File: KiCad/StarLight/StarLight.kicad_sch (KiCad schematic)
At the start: 17 parts, among them Q1 Q_NPN, Q2 Q_NPN, Q3 Q_NPN, SW1 SW, SW2 SW

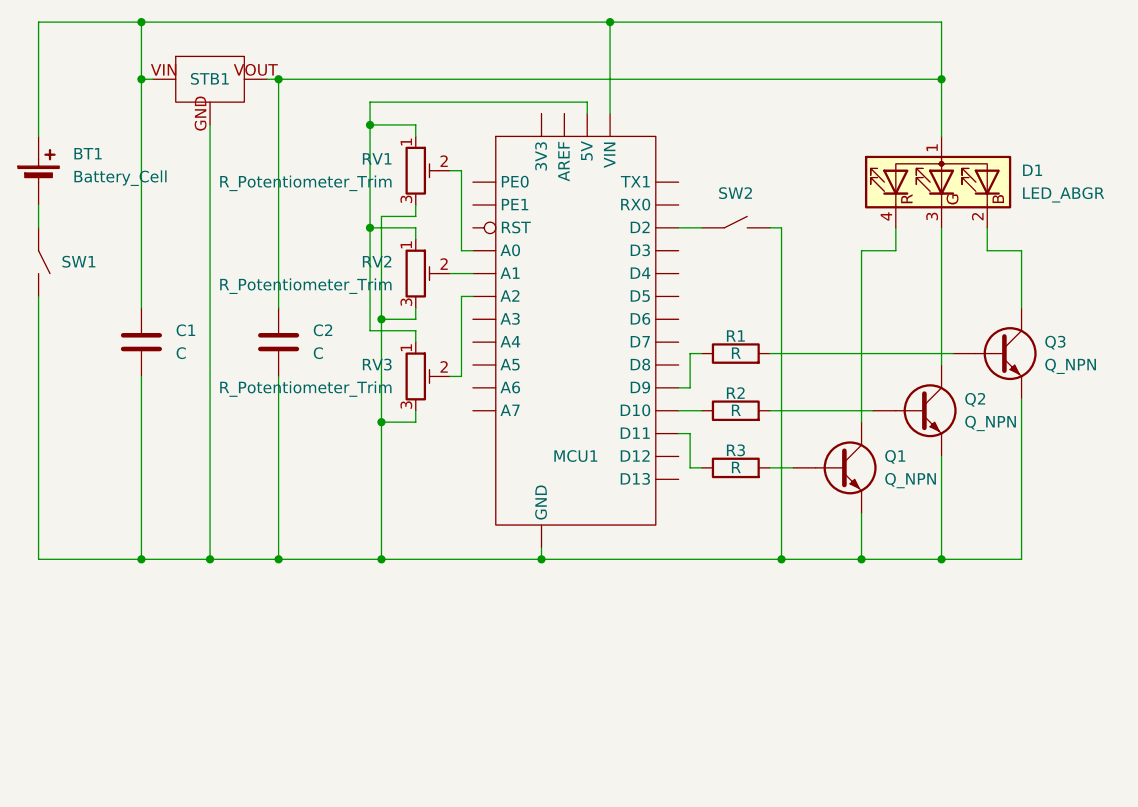
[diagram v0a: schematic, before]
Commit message: Create layout for elements
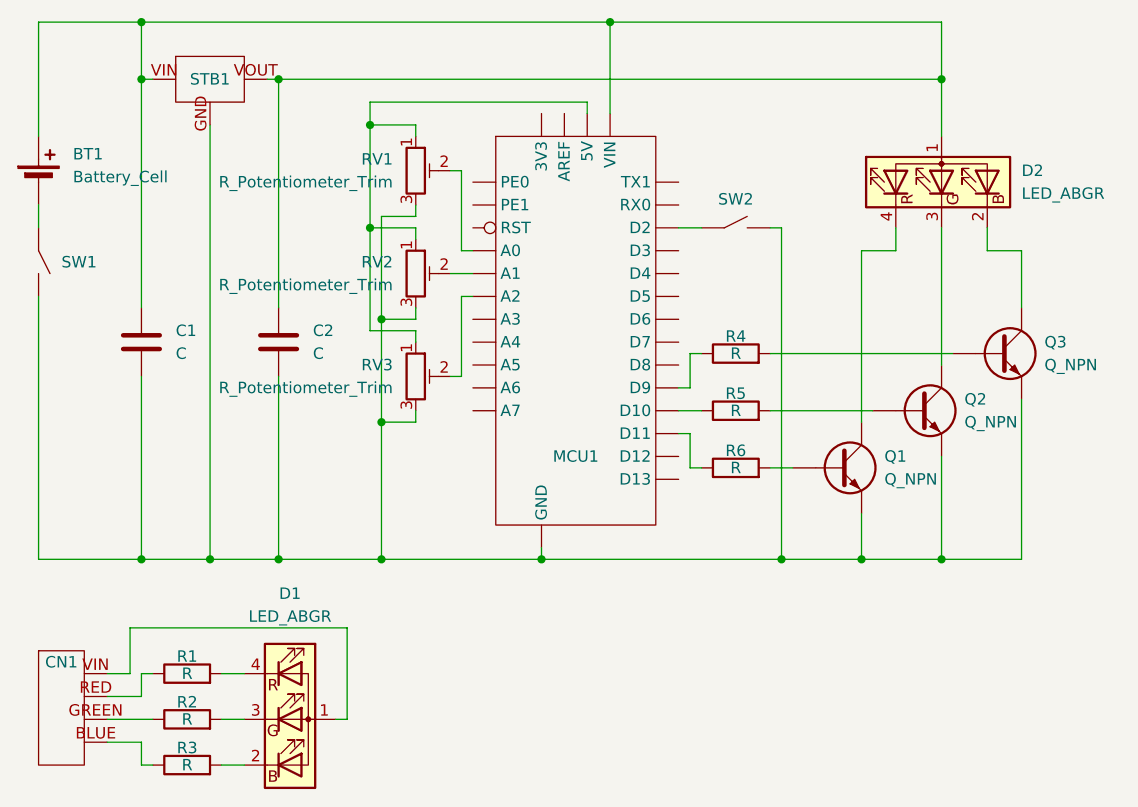
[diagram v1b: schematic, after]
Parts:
- added CN1: CN, StarLightLayouts:PLS-4, symbol StarLightSymbols:Connector
- added D1: LED_ABGR, StarLightLayouts:RGB led, symbol Device:LED_ABGR
- added R1, R5, R6: R, StarLightLayouts:Res THT 0.25W min, symbol Device:R
- BT1: footprint (none) -> StarLightLayouts:PLS-2; Href (none) -> https://roboshop.spb.ru/power/adaptery-pitaniya/vd-916-12v-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; Напряжение (none) -> 12; Ток (none) -> 2
- C1, C2: footprint (none) -> StarLightLayouts:Ceramic capacitor; Href (none) -> https://www.chipdip.ru/product/tajc106k016rnj-kondensator-a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; U (none) -> 12; С (none) -> 10 mk
- D2: renamed from D1; footprint (none) -> StarLightLayouts:PLS-4
- MCU1: Href (none) -> https://roboshop.spb.ru/arduino/kontrollery-arduino/arduino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
- Q1, Q2, Q3: footprint (none) -> StarLightLayouts:SOT23; F (none) -> 256; Href (none) -> https://www.chipdip.ru/product/pbss4350t-215-tranzistor-npn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; Ic (none) -> 0.24; Type (none) -> NPN; Vce (none) -> 5
- R2, R3: footprint (none) -> StarLightLayouts:Res THT 0.25W min; Href (none) -> https://www.chipdip.ru/product/cf-25-s1-4-0.25vt-62-om-5-re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; P (none) -> 0.024; R (none) -> 60
- R4: renamed from R1; footprint (none) -> StarLightLayouts:Res THT 0.25W min; Href (none) -> https://www.chipdip.ru/product/r1-173-2-5-1kom-5-1-rezistor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; P (none) -> 0.00304; R (none) -> 4750
- RV1, RV2, RV3: footprint (none) -> StarLightLayouts:PLS-3; Href (none) -> https://www.chipdip.ru/product/l-kls4-wh148-1a-2-18t-b103-l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; P (none) -> 0.25; R (none) -> 10k
- STB1: footprint (none) -> StarLightLayouts:SOT-223; Href (none) -> https://www.chipdip.ru/product/lm1117impx-adj-nopb-lineynyy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; Iout (none) -> 0.72; Vin (none) -> 12; Vout (none) -> 5
- SW1, SW2: footprint (none) -> StarLightLayouts:B2B-XH-A; Href (none) -> https://www.chipdip.ru/product/mts-102-a1-tumbler-on-on-3a-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; Напряжение (none) -> 12; Ток (none) -> 2
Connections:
- net at R2.1: now also CN1.GREEN; no longer MCU1.D10
- net at R2.2: now also D1.3 (GK); no longer Q2.B
- net at R3.1: now also CN1.BLUE; no longer MCU1.D11
- net at R3.2: now also D1.2 (BK); no longer Q1.B
- new net: CN1.RED, R1.1
- new net: CN1.VIN, D1.1 (A)
- new net: D1.4 (RK), R1.2
- new net: MCU1.D10, R5.1
- new net: MCU1.D11, R6.1
- new net: Q2.B, R5.2
- new net: Q1.B, R6.2

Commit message: Create layouts
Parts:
- MCU1: footprint (none) -> StarLightLayouts:Arduino Nano V3 Type C PBS
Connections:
- net at BT1.1 (+), C1.1, MCU1.VIN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: no longer C2.1, D2.1 (A), STB1.VOUT
- net at CN1.VIN: now also D1.VIN (A); no longer D1.1 (A)
- net at R3.2: now also D1.BLUE (BK); no longer D1.2 (BK)
- net at R2.2: now also D1.GREEN (GK); no longer D1.3 (GK)
- net at R1.2: now also D1.RED (RK); no longer D1.4 (RK)
- new net: C2.1, D2.1 (A), STB1.VOUT
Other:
- moved on the sheet: D1
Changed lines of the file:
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@@
-	)
-	(junction
-		(at 119.38 25.4)
-		(diameter 0)
-		(color 0 0 0 0)
 	)
 	(junction
@@
 	)
 	(junction
-		(at 82.55 19.05)
-		(diameter 0)
-		(color 0 0 0 0)
-	)
-	(junction
 		(at 45.72 78.74)
 		(diameter 0)
@@
 	(wire
 		(pts
-			(xy 119.38 25.4) (xy 119.38 19.05)
-		)
-		(stroke
-			(width 0)
-			(type default)
-		)
-	)
-	(wire
-		(pts
 			(xy 119.38 41.91) (xy 119.38 57.15)
 		)
@@
 		(pts
 			(xy 60.96 30.48) (xy 55.88 30.48)
-		)
-		(stroke
-			(width 0)
-			(type default)
-		)
-	)
-	(wire
-		(pts
-			(xy 82.55 19.05) (xy 119.38 19.05)
 		)
 		(stroke
@@
 	)
 	(symbol
+		(lib_name "LED_ABGR_1")
 		(lib_id "Device:LED_ABGR")
 		(at 46.99 96.52 0)
@@
 			)
 		)
-		(pin "2"
-		)
-		(pin "4"
-		)
-		(pin "1"
-		)
-		(pin "3"
+		(pin "VIN"
+		)
+		(pin "BLUE"
+		)
+		(pin "RED"
+		)
+		(pin "GREEN"
 		)
 		(instances
@@
 			)
 		)
-		(property "Footprint" ""
+		(property "Footprint" "StarLightLayouts:Arduino Nano V3 Type C PBS"
 			(at 69.85 31.75 0)
 			(effects

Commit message: replacement of seats
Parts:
- C1: С 10 mk -> 0.33 mk
- C2: С 10 mk -> 0.1 mk
- Q1, Q2, Q3: footprint StarLightLayouts:SOT23 -> StarLightLayouts:TO-92
- R1, R2, R3: footprint StarLightLayouts:Res THT 0.25W min -> StarLightLayouts:SMD 0805
- STB1: footprint StarLightLayouts:SOT-223 -> StarLightLayouts:TO-220
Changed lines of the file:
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@@
 			)
 		)
-		(property "С" "10 mk"
+		(property "С" "0.33 mk"
 			(at 30.48 54.61 0)
 			(effects
@@
 			)
 		)
-		(property "Footprint" "StarLightLayouts:SOT23"
+		(property "Footprint" "StarLightLayouts:TO-92"
 			(at 130.81 53.34 0)
 			(effects
@@
 			)
 		)
-		(property "Footprint" "StarLightLayouts:Res THT 0.25W min"
+		(property "Footprint" "StarLightLayouts:SMD 0805"
 			(at 35.56 98.298 90)
 			(effects
@@
 			)
 		)
-		(property "С" "10 mk"
+		(property "С" "0.1 mk"
 			(at 45.72 54.61 0)
 			(effects
@@
 			)
 		)
-		(property "Footprint" "StarLightLayouts:Res THT 0.25W min"
+		(property "Footprint" "StarLightLayouts:SMD 0805"
 			(at 35.56 93.218 90)
 			(effects
@@
 			)
 		)
-		(property "Footprint" "StarLightLayouts:SOT23"
+		(property "Footprint" "StarLightLayouts:TO-92"
 			(at 113.03 66.04 0)
 			(effects
@@
 			)
 		)
-		(property "Footprint" "StarLightLayouts:SOT23"
+		(property "Footprint" "StarLightLayouts:TO-92"
 			(at 121.92 59.69 0)
 			(effects
@@
 			)
 		)
-		(property "Footprint" "StarLightLayouts:Res THT 0.25W min"
+		(property "Footprint" "StarLightLayouts:SMD 0805"
 			(at 35.56 103.378 90)
 			(effects
@@
 			)
 		)
-		(property "Footprint" "StarLightLayouts:SOT-223"
+		(property "Footprint" "StarLightLayouts:TO-220"
 			(at 38.1 25.4 0)
 			(effects
